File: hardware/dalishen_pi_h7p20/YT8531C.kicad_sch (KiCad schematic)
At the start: 47 parts, among them J10 RJ45_HR911130A, U1 YT8531C, Y2 25M, 10PPM

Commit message: [dalishen_pi_h7p20] backup
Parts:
- R44: value 10k -> 10k,1%
- R45: value 2.49k,1% -> 2.49k
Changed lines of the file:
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@@
       (effects (font (size 1.27 1.27)) (justify left))
     )
-    (property "Value" "10k" (at 72.39 121.92 0)
+    (property "Value" "10k,1%" (at 72.39 121.92 0)
       (effects (font (size 1.27 1.27)) (justify left))
     )
@@
       (effects (font (size 1.27 1.27)) (justify left))
     )
-    (property "Value" "2.49k,1%" (at 78.74 40.64 0)
-      (effects (font (size 1.27 1.27)) (justify left))
-    )
+    (property "Value" "2.49k" (at 78.74 40.64 0)
+      (effects (font (size 1.27 1.27)) (justify left))
+    )

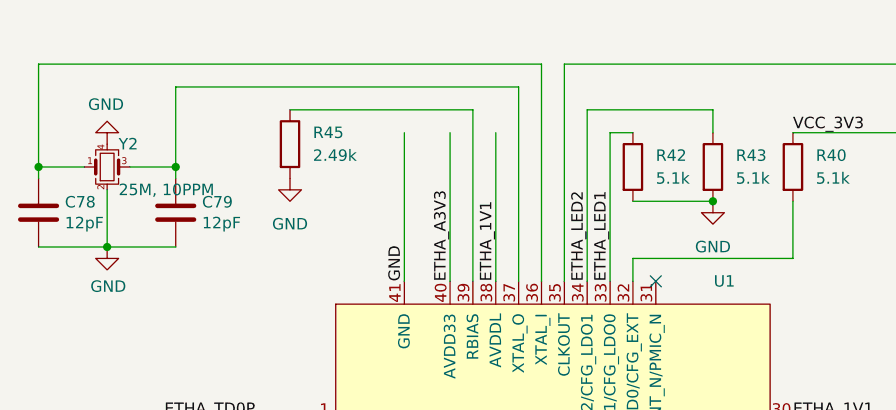
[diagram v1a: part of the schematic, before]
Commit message: [usb_sniffer_h7p20] USB3343兼容CH132F，作相关调整
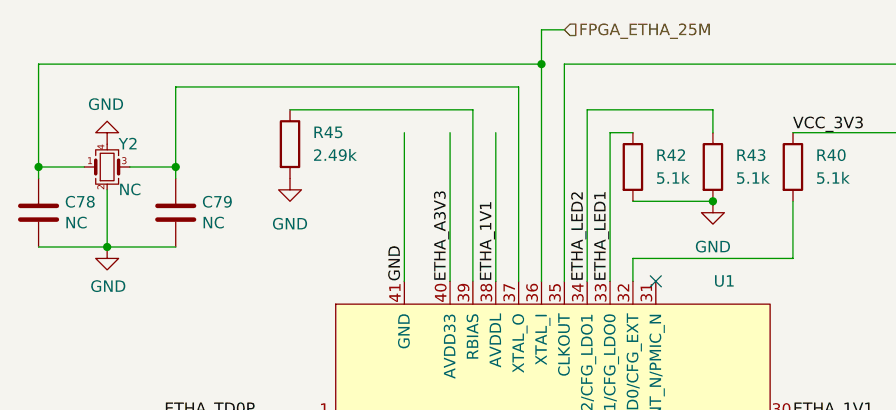
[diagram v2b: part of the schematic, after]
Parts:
- C78, C79: value 12pF -> NC
- Y2: value 25M, 10PPM -> NC
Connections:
- net FPGA_ETHA_25M: now reaches C78.2, U1.36 (XTAL_I), Y2.1
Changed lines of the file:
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@@
   (junction (at 130.81 163.83) (diameter 0) (color 0 0 0 0)
+  )
+  (junction (at 104.14 30.48) (diameter 0) (color 0 0 0 0)
   )
   (junction (at 162.56 106.68) (diameter 0) (color 0 0 0 0)
@@
     (stroke (width 0) (type default))
   )
+  (wire (pts (xy 104.14 26.67) (xy 104.14 30.48))
+    (stroke (width 0) (type default))
+  )
   (wire (pts (xy 111.76 38.1) (xy 114.3 38.1))
     (stroke (width 0) (type default))
@@
     (stroke (width 0) (type default))
   )
+  (wire (pts (xy 106.68 26.67) (xy 104.14 26.67))
+    (stroke (width 0) (type default))
+  )
   (wire (pts (xy 48.26 41.91) (xy 48.26 30.48))
     (stroke (width 0) (type default))
@@
   )
   (hierarchical_label "FPGA_ETHA_TXCLK" (shape input) (at 148.59 127 0) (fields_autoplaced)
+    (effects (font (size 1.27 1.27)) (justify left))
+  )
+  (hierarchical_label "FPGA_ETHA_25M" (shape input) (at 106.68 26.67 0) (fields_autoplaced)
     (effects (font (size 1.27 1.27)) (justify left))
   )
@@
       (effects (font (size 1.27 1.27)) (justify left))
     )
-    (property "Value" "25M, 10PPM" (at 57.15 44.45 0)
+    (property "Value" "NC" (at 57.15 44.45 0)
       (effects (font (size 1.27 1.27)) (justify left))
     )
@@
       (effects (font (size 1.27 1.27)) (justify right))
     )
-    (property "Value" "12pF" (at 51.181 48.133 0)
+    (property "Value" "NC" (at 51.181 48.133 0)
       (effects (font (size 1.27 1.27)) (justify right))
     )
@@
       (effects (font (size 1.27 1.27)) (justify right))
     )
-    (property "Value" "12pF" (at 66.421 48.133 0)
-      (effects (font (size 1.27 1.27)) (justify right))
-    )
+    (property "Value" "NC" (at 66.421 48.133 0)
+      (effects (font (size 1.27 1.27)) (justify right))
+    )

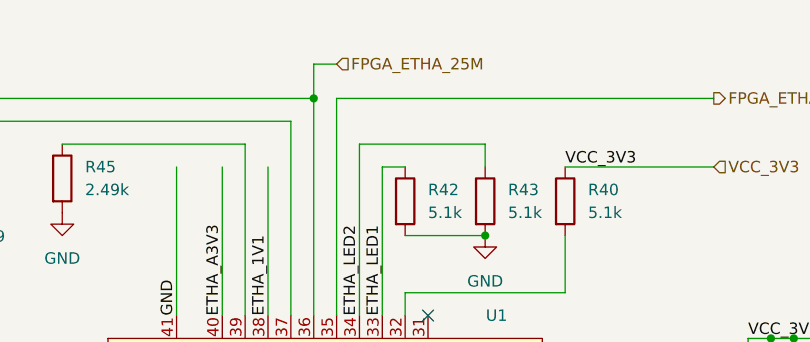
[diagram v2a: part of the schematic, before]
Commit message: [dalishen_pi_h7p20] 原理图初稿
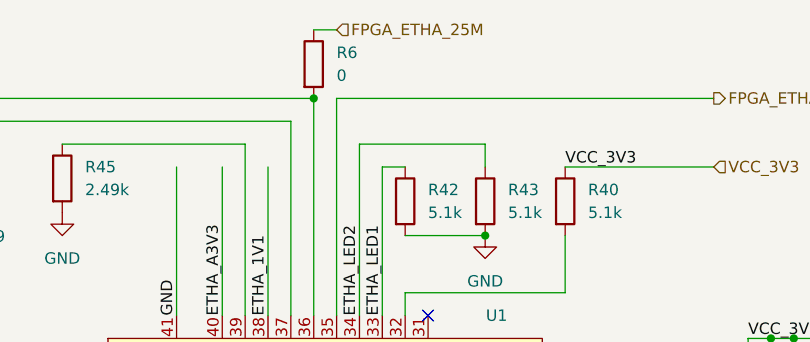
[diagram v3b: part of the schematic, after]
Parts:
- added R6: 0, Resistor_SMD:R_0402_1005Metric, symbol Device:R
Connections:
- net FPGA_ETHA_25M: now also R6.1; no longer C78.2, U1.36 (XTAL_I), Y2.1
- new net: C78.2, R6.2, U1.36 (XTAL_I), Y2.1
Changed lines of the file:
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@@
   (junction (at 99.06 182.88) (diameter 0) (color 0 0 0 0)
   )
+  (junction (at 104.14 30.48) (diameter 0) (color 0 0 0 0)
+  )
   (junction (at 162.56 82.55) (diameter 0) (color 0 0 0 0)
   )
@@
   )
   (junction (at 130.81 163.83) (diameter 0) (color 0 0 0 0)
-  )
-  (junction (at 104.14 30.48) (diameter 0) (color 0 0 0 0)
   )
   (junction (at 162.56 106.68) (diameter 0) (color 0 0 0 0)
@@
     (stroke (width 0) (type default))
   )
-  (wire (pts (xy 104.14 26.67) (xy 104.14 30.48))
-    (stroke (width 0) (type default))
-  )
   (wire (pts (xy 111.76 38.1) (xy 114.3 38.1))
     (stroke (width 0) (type default))
@@
     (stroke (width 0) (type default))
   )
-  (wire (pts (xy 106.68 26.67) (xy 104.14 26.67))
+  (wire (pts (xy 106.68 22.86) (xy 104.14 22.86))
     (stroke (width 0) (type default))
   )
@@
     (effects (font (size 1.27 1.27)) (justify left))
   )
-  (hierarchical_label "FPGA_ETHA_25M" (shape input) (at 106.68 26.67 0) (fields_autoplaced)
+  (hierarchical_label "FPGA_ETHA_25M" (shape input) (at 106.68 22.86 0) (fields_autoplaced)
     (effects (font (size 1.27 1.27)) (justify left))
   )
@@
         )
       )
+    )
+  )
+  (symbol (lib_id "Device:R") (at 104.14 26.67 0) (unit 1)
+    (in_bom yes) (on_board yes) (dnp no) (fields_autoplaced)
+    (property "Reference" "R6" (at 106.68 25.4 0)
+      (effects (font (size 1.27 1.27)) (justify left))
+    )
+    (property "Value" "0" (at 106.68 27.94 0)
+      (effects (font (size 1.27 1.27)) (justify left))
+    )
+    (property "Footprint" "Resistor_SMD:R_0402_1005Metric" (at 102.362 26.67 90)
+      (effects (font (size 1.27 1.27)) hide)
+    )
+    (property "Datasheet" "~" (at 104.14 26.67 0)
+      (effects (font (size 1.27 1.27)) hide)
+    )
+    (pin "2")
+    (pin "1")
+    (instances
+      (project "dalishen_pi_h7p20"
+        (path "/221176f3-b6da-4f04-afa6-f8c6dd49907a/68d888d9-8902-4de5-b39b-ba860add9831"
+          (reference "R6") (unit 1)
+        )
+      )

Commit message: [dalishen_pi_h7p20] layout done
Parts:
- R41: value 5.1k -> 4.7k
- R54: value NC -> 5.1k
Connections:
- net FPGA_ETHA_RXCK: no longer R46.2
- net FPGA_ETHA_RXCTL: no longer R47.2
- net FPGA_ETHA_RXD3: no longer R48.2
- net GND: now also R46.2, R47.2
- net VCC_3V3: no longer R46.1, R47.1
- net at R75.2, U1.22 (RXD3/PHYAD0): now also R48.2
- net at R71.2, U1.26 (RX_CTL/PHYAD2): now also R47.1
- net at R70.2, U1.27 (RX_CLK/PHYAD1): now also R46.1
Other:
- moved on the sheet: C47, C48, C51, C52, C53, C55, C57, C58, C59, C60, C78, C79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

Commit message: [dalishen_pi_h7p20] 样板
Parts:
- R38, R39: value 5.1k -> 2.49k
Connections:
- net ETHA_LED1: now also J10.14; no longer J10.11
- net ETHA_LED2: now also J10.11; no longer J10.14
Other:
- moved on the sheet: R38, R39
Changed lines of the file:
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@@
   (junction (at 63.5 161.29) (diameter 0) (color 0 0 0 0)
   )
-  (junction (at 212.09 74.93) (diameter 0) (color 0 0 0 0)
+  (junction (at 212.09 71.12) (diameter 0) (color 0 0 0 0)
   )
   (junction (at 99.06 43.18) (diameter 0) (color 0 0 0 0)
@@
     (stroke (width 0) (type default))
   )
-  (wire (pts (xy 241.3 74.93) (xy 241.3 77.47))
+  (wire (pts (xy 241.3 71.12) (xy 241.3 77.47))
     (stroke (width 0) (type default))
   )
@@
     (stroke (width 0) (type default))
   )
+  (wire (pts (xy 236.22 73.66) (xy 236.22 77.47))
+    (stroke (width 0) (type default))
+  )
   (wire (pts (xy 148.59 80.01) (xy 148.59 92.71))
     (stroke (width 0) (type default))
@@
     (stroke (width 0) (type default))
   )
-  (wire (pts (xy 212.09 74.93) (xy 215.9 74.93))
+  (wire (pts (xy 212.09 71.12) (xy 215.9 71.12))
     (stroke (width 0) (type default))
   )
@@
     (stroke (width 0) (type default))
   )
-  (wire (pts (xy 212.09 72.39) (xy 212.09 74.93))
+  (wire (pts (xy 212.09 73.66) (xy 212.09 71.12))
     (stroke (width 0) (type default))
   )
@@
     (stroke (width 0) (type default))
   )
+  (wire (pts (xy 107.95 33.02) (xy 107.95 35.56))
+    (stroke (width 0) (type default))
+  )
   (wire (pts (xy 39.37 30.48) (xy 39.37 39.37))
     (stroke (width 0) (type default))
@@
     (stroke (width 0) (type default))
   )
-  (wire (pts (xy 223.52 72.39) (xy 236.22 72.39))
+  (wire (pts (xy 223.52 73.66) (xy 236.22 73.66))
     (stroke (width 0) (type default))
   )
@@
     (stroke (width 0) (type default))
   )
-  (wire (pts (xy 215.9 72.39) (xy 212.09 72.39))
+  (wire (pts (xy 215.9 73.66) (xy 212.09 73.66))
     (stroke (width 0) (type default))
   )
@@
     (stroke (width 0) (type default))
   )
-  (wire (pts (xy 236.22 72.39) (xy 236.22 77.47))
-    (stroke (width 0) (type default))
-  )
   (wire (pts (xy 72.39 124.46) (xy 72.39 144.78))
     (stroke (width 0) (type default))
@@
     (stroke (width 0) (type default))
   )
-  (wire (pts (xy 223.52 74.93) (xy 241.3 74.93))
+  (wire (pts (xy 223.52 71.12) (xy 241.3 71.12))
     (stroke (width 0) (type default))
   )
@@
     (stroke (width 0) (type default))
   )
-  (wire (pts (xy 107.95 35.56) (xy 124.46 35.56))
+  (wire (pts (xy 107.95 33.02) (xy 124.46 33.02))
     (stroke (width 0) (type default))
   )
@@
     (effects (font (size 1.27 1.27)) (justify left bottom))
   )
-  (label "ETHA_LED2" (at 212.09 68.58 0) (fields_autoplaced)
+  (label "ETHA_LED2" (at 212.09 64.77 0) (fields_autoplaced)
     (effects (font (size 1.27 1.27)) (justify left bottom))
   )
@@
     (effects (font (size 1.27 1.27)) (justify left bottom))
   )
-  (label "ETHA_LED1" (at 212.09 64.77 0) (fields_autoplaced)
+  (label "ETHA_LED1" (at 212.09 68.58 0) (fields_autoplaced)
     (effects (font (size 1.27 1.27)) (justify left bottom))
   )
@@
     (effects (font (size 1.27 1.27)) (justify left bottom))
   )
-  (label "VCC_3V3" (at 107.95 35.56 0) (fields_autoplaced)
+  (label "VCC_3V3" (at 107.95 33.02 0) (fields_autoplaced)
     (effects (font (size 1.27 1.27)) (justify left bottom))
   )
@@
     (effects (font (size 1.27 1.27)) (justify left))
   )
-  (hierarchical_label "VCC_3V3" (shape input) (at 124.46 35.56 0) (fields_autoplaced)
+  (hierarchical_label "VCC_3V3" (shape input) (at 124.46 33.02 0) (fields_autoplaced)
     (effects (font (size 1.27 1.27)) (justify left))
   )
@@
     )
   )
-  (symbol (lib_id "Device:R") (at 219.71 74.93 270) (unit 1)
-    (in_bom yes) (on_board yes) (dnp no)
-    (property "Reference" "R39" (at 224.79 73.66 90)
-      (effects (font (size 1.27 1.27)))
-    )
-    (property "Value" "5.1k" (at 219.71 74.93 90)
-      (effects (font (size 1.27 1.27)))
-    )
-    (property "Footprint" "Resistor_SMD:R_0402_1005Metric" (at 219.71 73.152 90)
-      (effects (font (size 1.27 1.27)) hide)
-    )
-    (property "Datasheet" "~" (at 219.71 74.93 0)
+  (symbol (lib_id "Device:R") (at 219.71 71.12 270) (unit 1)
+    (in_bom yes) (on_board yes) (dnp no)
+    (property "Reference" "R39" (at 224.79 69.85 90)
+      (effects (font (size 1.27 1.27)))
+    )
+    (property "Value" "2.49k" (at 219.71 71.12 90)
+      (effects (font (size 1.27 1.27)))
+    )
+    (property "Footprint" "Resistor_SMD:R_0402_1005Metric" (at 219.71 69.342 90)
+      (effects (font (size 1.27 1.27)) hide)
+    )
+    (property "Datasheet" "~" (at 219.71 71.12 0)
       (effects (font (size 1.27 1.27)) hide)
     )
@@
     )
   )
-  (symbol (lib_id "power:GND") (at 212.09 74.93 270) (unit 1)
-    (in_bom yes) (on_board yes) (dnp no)
-    (property "Reference" "#PWR042" (at 205.74 74.93 0)
-      (effects (font (size 1.27 1.27)) hide)
-    )
-    (property "Value" "GND" (at 204.47 74.93 90)
-      (effects (font (size 1.27 1.27)) (justify left))
-    )
-    (property "Footprint" "" (at 212.09 74.93 0)
-      (effects (font (size 1.27 1.27)) hide)
-    )
-    (property "Datasheet" "" (at 212.09 74.93 0)
+  (symbol (lib_id "power:GND") (at 212.09 71.12 270) (unit 1)
+    (in_bom yes) (on_board yes) (dnp no)
+    (property "Reference" "#PWR042" (at 205.74 71.12 0)
+      (effects (font (size 1.27 1.27)) hide)
+    )
+    (property "Value" "GND" (at 204.47 71.12 90)
+      (effects (font (size 1.27 1.27)) (justify left))
+    )
+    (property "Footprint" "" (at 212.09 71.12 0)
+      (effects (font (size 1.27 1.27)) hide)
+    )
+    (property "Datasheet" "" (at 212.09 71.12 0)
       (effects (font (size 1.27 1.27)) hide)
     )
@@
     )
   )
-  (symbol (lib_id "Device:R") (at 219.71 72.39 270) (unit 1)
-    (in_bom yes) (on_board yes) (dnp no)
-    (property "Reference" "R38" (at 224.79 71.12 90)
-      (effects (font (size 1.27 1.27)))
-    )
-    (property "Value" "5.1k" (at 219.71 72.39 90)
-      (effects (font (size 1.27 1.27)))
-    )
-    (property "Footprint" "Resistor_SMD:R_0402_1005Metric" (at 219.71 70.612 90)
-      (effects (font (size 1.27 1.27)) hide)
-    )
-    (property "Datasheet" "~" (at 219.71 72.39 0)
-      (effects (font (size 1.27 1.27)) hide)
-    )
+  (symbol (lib_id "Device:R") (at 219.71 73.66 270) (unit 1)
+    (in_bom yes) (on_board yes) (dnp no)
+    (property "Reference" "R38" (at 224.79 72.39 90)
+      (effects (font (size 1.27 1.27)))
+    )
+    (property "Value" "2.49k" (at 219.71 73.66 90)
+      (effects (font (size 1.27 1.27)))
+    )
+    (property "Footprint" "Resistor_SMD:R_0402_1005Metric" (at 219.71 71.882 90)
+      (effects (font (size 1.27 1.27)) hide)
+    )
+    (property "Datasheet" "~" (at 219.71 73.66 0)
+      (effects (font (size 1.27 1.27)) hide)
+    )

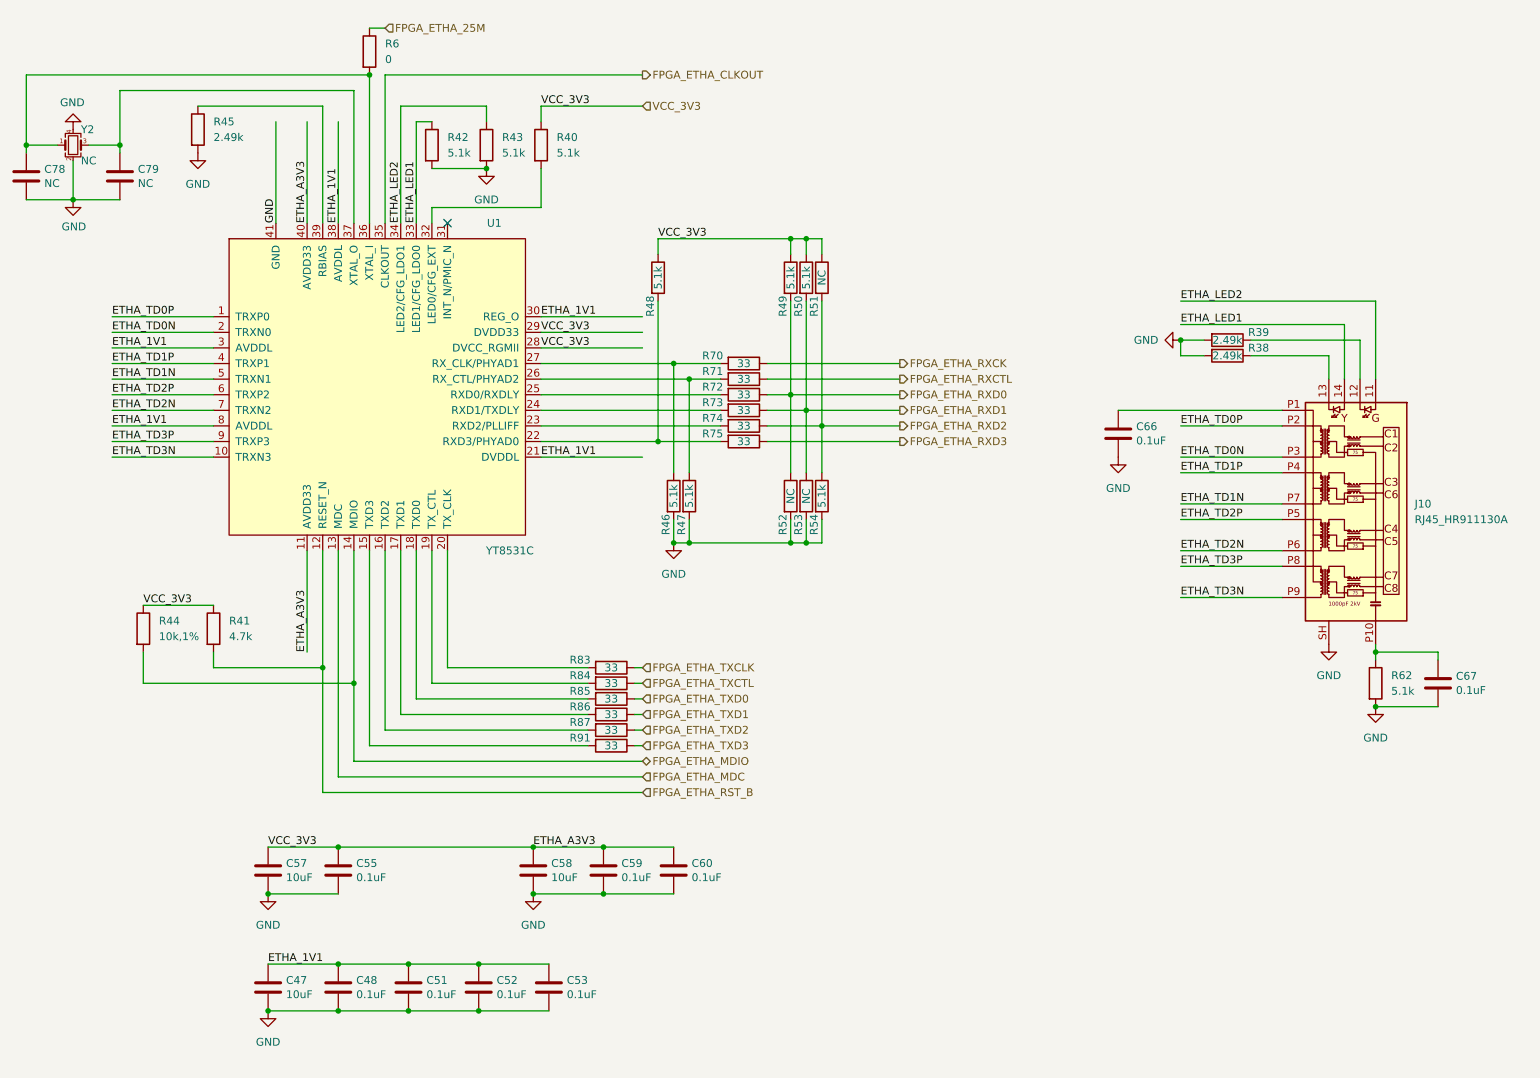
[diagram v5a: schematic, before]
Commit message: [dalishen_pi_h7p20] YT8531C需增加一个电感；需从XO引入时钟，XI接地； 剩余样板需换贴YC8531DC或者手工割线加电感。千兆协商通过。 LAYOUT优化
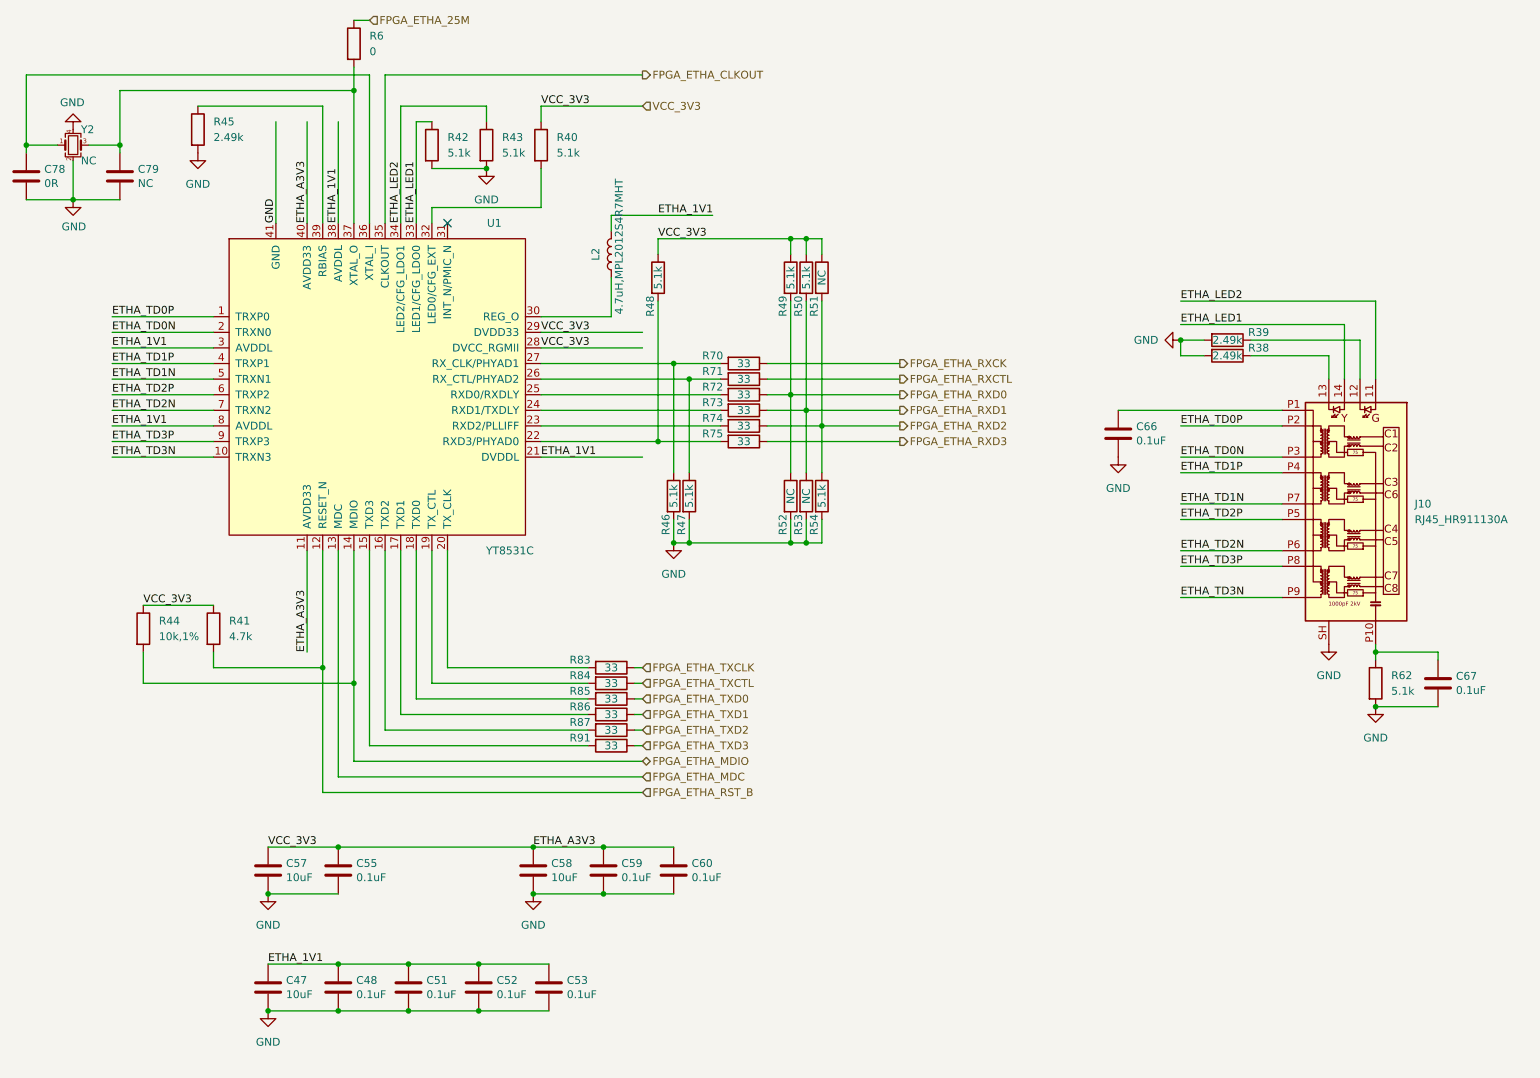
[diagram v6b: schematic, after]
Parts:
- added L2: 4.7uH,MPL2012S4R7MHT, Inductor_SMD:L_0805_2012Metric, symbol Device:L
- C78: value NC -> 0R
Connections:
- net ETHA_1V1: now also L2.2; no longer U1.30 (REG_O)
- net at C78.2, U1.36 (XTAL_I), Y2.1: no longer R6.2
- net at C79.2, U1.37 (XTAL_O), Y2.3: now also R6.2
- new net: L2.1, U1.30 (REG_O)
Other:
- moved on the sheet: R6
